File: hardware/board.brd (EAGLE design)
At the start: 53 x 30 mm, 45 parts, among them IC1 0915BM15A0001, J1 U.FL, U3 BLE113-A, X1 24MHz 8pF 10ppm -20C +70C, X3 MINI-USB-UX60-MB-5ST

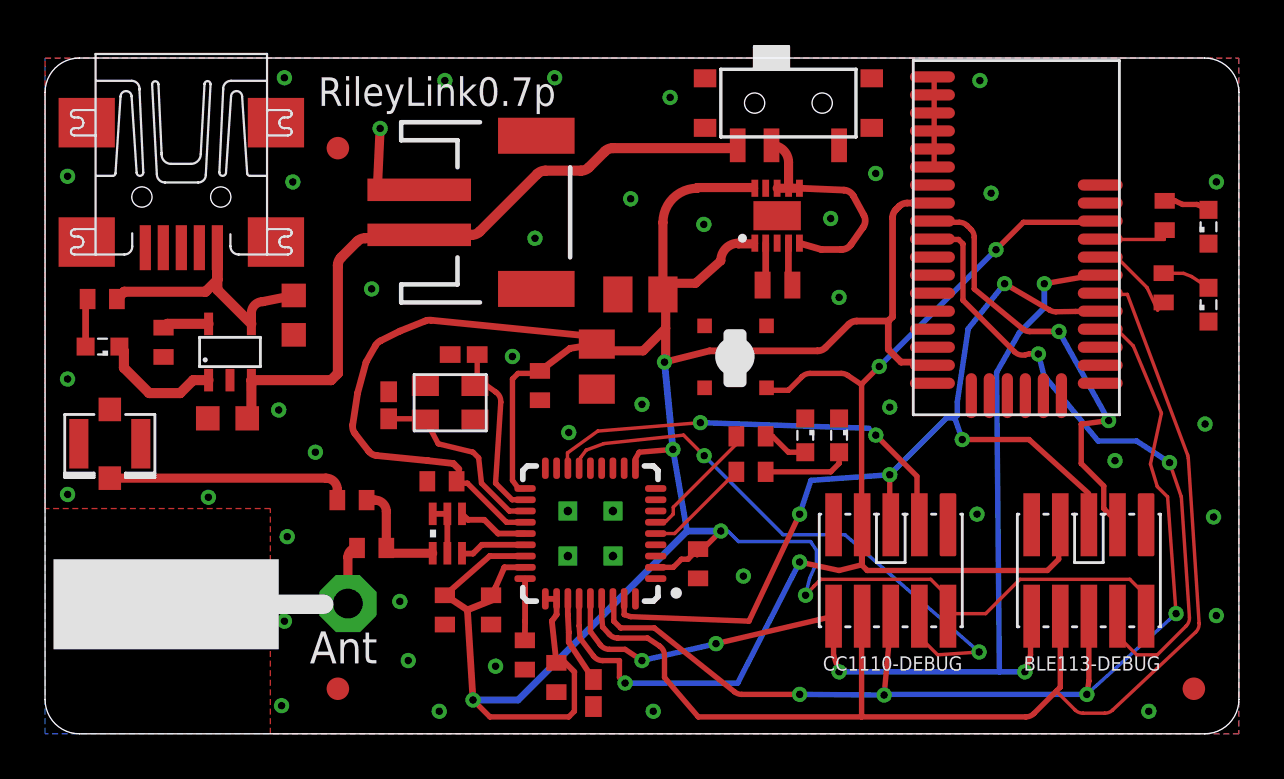
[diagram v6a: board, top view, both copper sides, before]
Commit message: New layout for voltage regulator, add 2 pin header for alternate power.
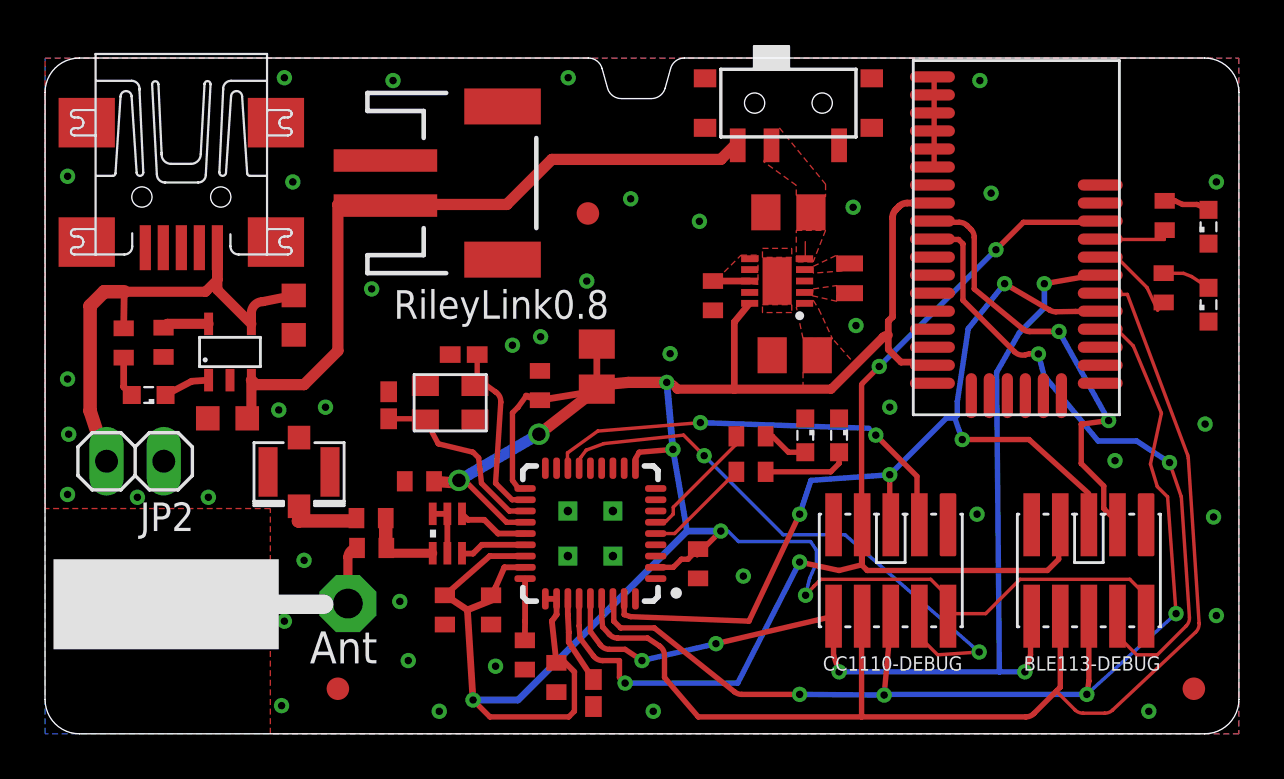
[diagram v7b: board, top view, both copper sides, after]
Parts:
- removed U$2: TACTILE_SWITCH, parts:PTS540
- added C14: 0.1uF, rcl:C0402
- added C15: 10 uF, rcl:C0805K
- added JP2: (no value), pinhead:1X02
- moved FID2 11.5 mm to (24.1, 23.1)
- moved J1 8.49 mm to (11.3, 11.6)
- moved C4 7.36 mm to (33.3, 16.8)
- moved L1 3.21 mm to (35.7, 20.2), turned to 90 degrees
- moved LED1 2.97 mm to (4.60, 15.0)
- moved REGULATOR 2.90 mm to (32.5, 20.1), turned to 180 degrees
- moved R2 2.17 mm to (3.49, 17.4), turned to 270 degrees
- moved JP1 1.98 mm to (18.8, 24.4)
- moved R4 1.17 mm to (14.5, 9.57)
- moved C13 1.00 mm to (16.6, 11.2)
- turned C11 to 90 degrees
- turned C12 to 90 degrees
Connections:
- new net N$13: C14.2, REGULATOR.6, REGULATOR.7, REGULATOR.8
- net GND: now also C14.1, C15.1, JP2.1; no longer U$2.P$4
- net RESET: no longer U$2.P$2
- net V+: now also C15.2; no longer REGULATOR.6, REGULATOR.7, REGULATOR.8
- net VIN_USB: now also JP2.2
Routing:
- net VDD: track 151.7 -> 127.5 mm, vias 5 -> 7
- net VIN_USB: track 12.8 -> 22.8 mm
- net V+: track 10.5 -> 0.77 mm
- net N$9: track 10.8 -> 3.29 mm
- net RESET: track 58.2 -> 53.5 mm
- net GND: track 11.6 -> 7.00 mm, vias 41 -> 40
- net N$2: track 5.49 -> 2.06 mm
- net N$6: track 2.38 -> 0.00 mm
- net N$1: track 1.92 -> 0.00 mm
- net N$13: track 0.00 -> 1.63 mm
- net N$10: track 4.94 -> 3.57 mm
- net VBAT: track 30.4 -> 31.7 mm
- added copper zone on layer 1, net N$1
- added copper zone on layer 1, net N$13
- added copper zone on layer 1, net N$6
- added copper zone on layer 1, net V+
- added copper zone on layer 1, net VDD
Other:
- outline, holes or cut-outs redrawn
- board text added: "RileyLink0.8"
- board text removed: "RileyLink0.7p"

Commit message: Adding higher rated inductor
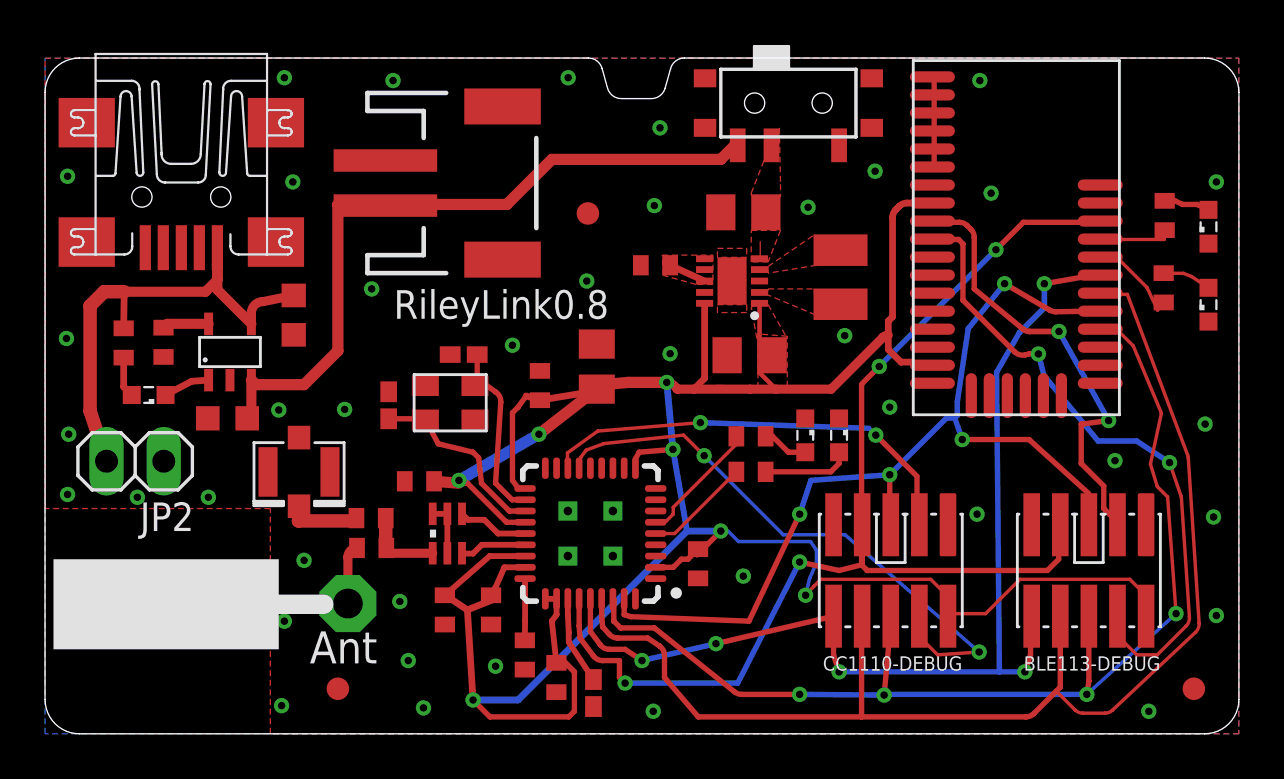
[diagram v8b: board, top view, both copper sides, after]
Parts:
- L1: device Bourns_By_element14_Batch_1:INDC1610X12N -> rcl:L2825P
- moved C14 2.89 mm to (27.1, 20.8), turned to 0 degrees
- moved C15 2.00 mm to (31.0, 23.1)
- moved C4 2.00 mm to (31.3, 16.8)
- moved REGULATOR 2.00 mm to (30.5, 20.1)
- moved L1 0.40 mm to (35.3, 20.3)
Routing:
- net VDD: track 127.5 -> 130.4 mm
